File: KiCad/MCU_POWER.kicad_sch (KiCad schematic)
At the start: 12 parts, among them IC3 LDO40LPU33RY, J1 USB_B, J2 Jack-DC

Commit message: Board layout preleminary complete.
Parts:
- D3: footprint (none) -> Diode_SMD:D_SOD-123
- J2: footprint (none) -> Connector_BarrelJack:BarrelJack_CUI_PJ-063AH_Horizontal_CircularHoles
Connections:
- net RAW_FILTER: now reaches C11.1, D1.1 (K), D2.1 (K), D3.1 (K), FB1.1
- net USB_OUT: now reaches D1.2 (A), J1.1 (VBUS)
- net JACK_OUT: now reaches D2.2 (A), J2.1
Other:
- moved on the sheet: J2
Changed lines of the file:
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@@
   (no_connect (at 76.708 81.026))
   (no_connect (at 76.708 83.566))
-  (wire (pts (xy 77.724 111.252) (xy 76.2 111.252))
-    (stroke (width 0) (type default))
-  )
-  (wire (pts (xy 78.359 106.172) (xy 76.2 106.172))
+  (wire (pts (xy 74.803 106.172) (xy 78.359 106.172))
+    (stroke (width 0) (type default))
+  )
+  (wire (pts (xy 76.327 111.252) (xy 74.803 111.252))
     (stroke (width 0) (type default))
   )
@@
     (effects (font (size 3 3)) (justify left bottom))
   )
+  (label "JACK_OUT" (at 75.311 106.172 0) (fields_autoplaced)
+    (effects (font (size 0.7 0.7)) (justify left bottom))
+  )
+  (label "RAW_FILTER" (at 118.999 75.946 0) (fields_autoplaced)
+    (effects (font (size 1.27 1.27)) (justify left bottom))
+  )
   (label "EN" (at 160.528 73.406 0) (fields_autoplaced)
     (effects (font (size 0.8 0.8)) (justify left bottom))
+  )
+  (label "USB_OUT" (at 77.47 75.946 0) (fields_autoplaced)
+    (effects (font (size 0.7 0.7)) (justify left bottom))
   )
   (label "VIN" (at 160.02 75.946 0) (fields_autoplaced)
@@
       (effects (font (size 1.27 1.27)) (justify left))
     )
-    (property "Footprint" "" (at 100.076 79.756 0)
+    (property "Footprint" "Diode_SMD:D_SOD-123" (at 100.076 79.756 0)
       (effects (font (size 1.27 1.27)) hide)
     )
@@
   )
   (symbol (lib_id "Device:D_Schottky") (at 82.169 106.172 180) (unit 1)
-    (in_bom yes) (on_board yes) (dnp no) (fields_autoplaced)
-    (property "Reference" "D2" (at 82.4865 100.711 0)
-      (effects (font (size 1.27 1.27)))
-    )
-    (property "Value" "D_Schottky" (at 82.4865 103.251 0)
+    (in_bom yes) (on_board yes) (dnp no)
+    (property "Reference" "D2" (at 85.09 100.965 0)
+      (effects (font (size 1.27 1.27)))
+    )
+    (property "Value" "D_Schottky" (at 84.963 103.505 0)
       (effects (font (size 1.27 1.27)))
     )
@@
     )
   )
-  (symbol (lib_id "power:GND") (at 77.724 111.252 0) (unit 1)
-    (in_bom yes) (on_board yes) (dnp no) (fields_autoplaced)
-    (property "Reference" "#PWR014" (at 77.724 117.602 0)
-      (effects (font (size 1.27 1.27)) hide)
-    )
-    (property "Value" "GND" (at 77.724 115.824 0)
-      (effects (font (size 1.27 1.27)))
-    )
-    (property "Footprint" "" (at 77.724 111.252 0)
-      (effects (font (size 1.27 1.27)) hide)
-    )
-    (property "Datasheet" "" (at 77.724 111.252 0)
+  (symbol (lib_id "power:GND") (at 76.327 111.252 0) (unit 1)
+    (in_bom yes) (on_board yes) (dnp no) (fields_autoplaced)
+    (property "Reference" "#PWR014" (at 76.327 117.602 0)
+      (effects (font (size 1.27 1.27)) hide)
+    )
+    (property "Value" "GND" (at 76.327 115.824 0)
+      (effects (font (size 1.27 1.27)))
+    )
+    (property "Footprint" "" (at 76.327 111.252 0)
+      (effects (font (size 1.27 1.27)) hide)
+    )
+    (property "Datasheet" "" (at 76.327 111.252 0)
       (effects (font (size 1.27 1.27)) hide)
     )
@@
     )
   )
-  (symbol (lib_id "Connector:Jack-DC") (at 68.58 108.712 0) (unit 1)
-    (in_bom yes) (on_board yes) (dnp no) (fields_autoplaced)
-    (property "Reference" "J2" (at 68.58 101.219 0)
-      (effects (font (size 1.27 1.27)))
-    )
-    (property "Value" "Jack-DC" (at 68.58 103.759 0)
-      (effects (font (size 1.27 1.27)))
-    )
-    (property "Footprint" "" (at 69.85 109.728 0)
-      (effects (font (size 1.27 1.27)) hide)
-    )
-    (property "Datasheet" "~" (at 69.85 109.728 0)
-      (effects (font (size 1.27 1.27)) hide)
-    )
+  (symbol (lib_id "Connector:Jack-DC") (at 67.183 108.712 0) (unit 1)
+    (in_bom yes) (on_board yes) (dnp no) (fields_autoplaced)
+    (property "Reference" "J2" (at 67.183 101.219 0)
+      (effects (font (size 1.27 1.27)))
+    )
+    (property "Value" "Jack-DC" (at 67.183 103.759 0)
+      (effects (font (size 1.27 1.27)))
+    )
+    (property "Footprint" "Connector_BarrelJack:BarrelJack_CUI_PJ-063AH_Horizontal_CircularHoles" (at 68.453 109.728 0)
+      (effects (font (size 1.27 1.27)) hide)
+    )
+    (property "Datasheet" "~" (at 68.453 109.728 0)
+      (effects (font (size 1.27 1.27)) hide)
+    )

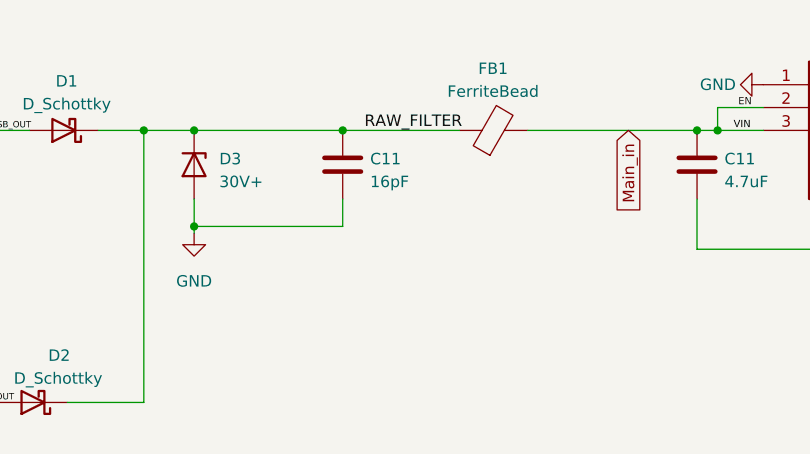
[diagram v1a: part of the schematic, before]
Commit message: Added some notes and extra ground vias.
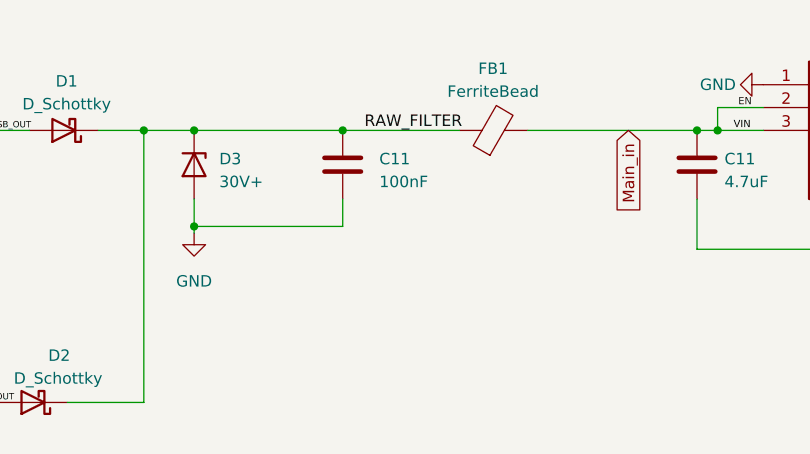
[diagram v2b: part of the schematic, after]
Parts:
- C11: value 16pF -> 100nF
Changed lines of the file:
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@@
   (symbol (lib_id "Device:C") (at 116.586 79.756 0) (unit 1)
     (in_bom yes) (on_board yes) (dnp no) (fields_autoplaced)
-    (property "Reference" "C11" (at 119.634 79.121 0)
+    (property "Reference" "C11" (at 120.65 79.121 0)
       (effects (font (size 1.27 1.27)) (justify left))
     )
-    (property "Value" "16pF" (at 119.634 81.661 0)
+    (property "Value" "100nF" (at 120.65 81.661 0)
       (effects (font (size 1.27 1.27)) (justify left))
     )

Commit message: Starting revision 1.1
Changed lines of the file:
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@@
   (junction (at 67.818 91.186) (diameter 0) (color 0 0 0 0)
+  )
+  (junction (at 194.564 75.946) (diameter 0) (color 0 0 0 0)
   )
   (junction (at 201.676 75.946) (diameter 0) (color 0 0 0 0)
@@
   (no_connect (at 76.708 81.026))
   (no_connect (at 76.708 83.566))
+  (wire (pts (xy 194.564 76.2) (xy 194.564 75.946))
+    (stroke (width 0) (type default))
+  )
   (wire (pts (xy 74.803 106.172) (xy 78.359 106.172))
     (stroke (width 0) (type default))
@@
     (stroke (width 0) (type default))
   )
-  (wire (pts (xy 201.676 75.946) (xy 197.358 75.946))
-    (stroke (width 0) (type default))
-  )
   (wire (pts (xy 67.818 91.186) (xy 69.088 91.186))
     (stroke (width 0) (type default))
@@
   )
   (wire (pts (xy 158.242 73.406) (xy 158.242 75.946))
+    (stroke (width 0) (type default))
+  )
+  (wire (pts (xy 197.358 75.946) (xy 201.676 75.946))
     (stroke (width 0) (type default))
   )
@@
   )
   (wire (pts (xy 178.562 89.154) (xy 178.562 88.646))
+    (stroke (width 0) (type default))
+  )
+  (wire (pts (xy 194.564 75.946) (xy 193.802 75.946))
     (stroke (width 0) (type default))
   )
@@
     (stroke (width 0) (type default))
   )
-  (wire (pts (xy 197.358 75.946) (xy 193.802 75.946))
+  (wire (pts (xy 197.358 75.946) (xy 194.564 75.946))
     (stroke (width 0) (type default))
   )
@@
     (effects (font (size 1.27 1.27)) (justify left bottom))
   )
-  (label "Vout" (at 199.39 75.946 0) (fields_autoplaced)
+  (label "Vout" (at 194.564 76.2 0) (fields_autoplaced)
     (effects (font (size 1.27 1.27)) (justify left bottom))
   )

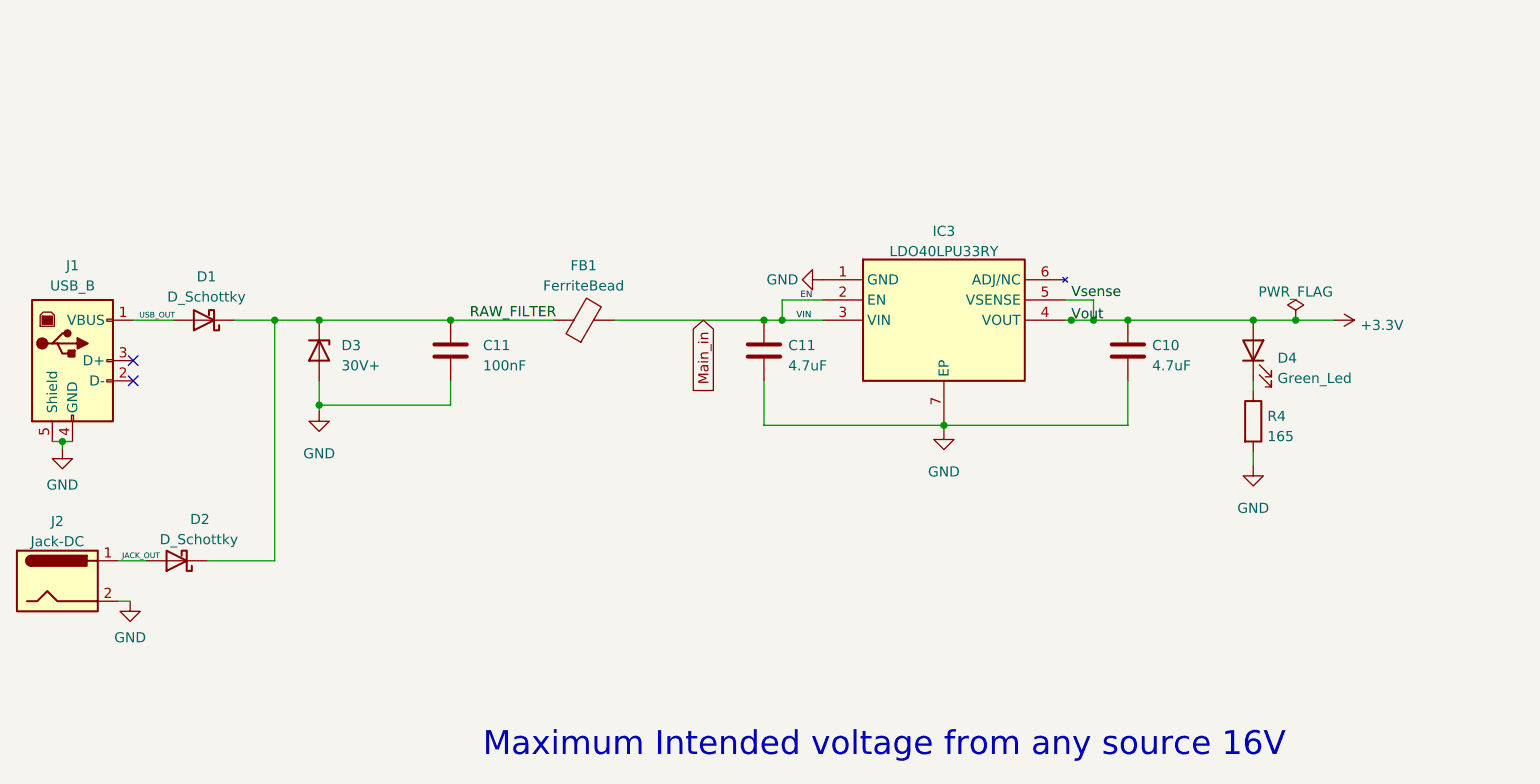
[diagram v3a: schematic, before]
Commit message: pushing ofr system reset
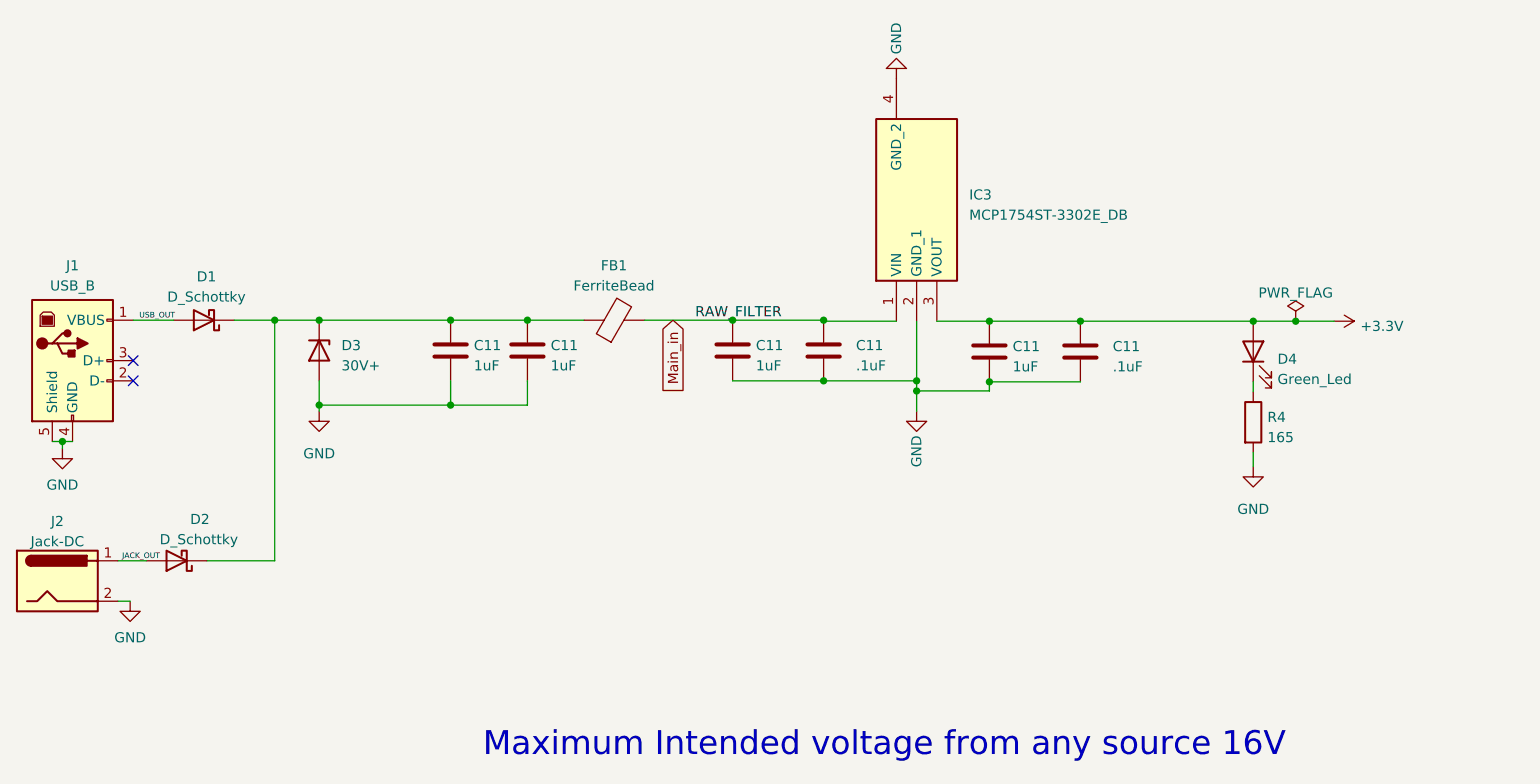
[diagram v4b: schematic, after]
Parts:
- removed C10, C11: 4.7uF, Capacitor_SMD:C_0603_1608Metric_Pad1.08x0.95mm_HandSolder, symbol Device:C
- removed C11: 100nF, Capacitor_SMD:C_0603_1608Metric_Pad1.08x0.95mm_HandSolder, symbol Device:C
- removed IC3: LDO40LPU33RY, Custom_eric:SON95P300X300X90-7N-D, symbol Custom_Eric:LDO40LPU33RY
- added C11 (x2): .1uF, Capacitor_SMD:C_0603_1608Metric_Pad1.08x0.95mm_HandSolder, symbol Device:C
- added C11 (x4): 1uF, Capacitor_SMD:C_0603_1608Metric_Pad1.08x0.95mm_HandSolder, symbol Device:C
- added IC3: MCP1754ST-3302E_DB, Custom_eric:MCP1754ST-3302E_DB, symbol Custom_eric:MCP1754ST-3302E_DB
- R4: footprint Resistor_SMD:R_0402_1005Metric_Pad0.72x0.64mm_HandSolder -> Resistor_SMD:R_0805_2012Metric_Pad1.20x1.40mm_HandSolder
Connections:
- net +3.3V: now also C11.1, C11.1, IC3.3 (VOUT)
- net GND: now also C11.2, C11.2, C11.2, C11.2, C11.2, C11.2, IC3.2 (GND_1), IC3.4 (GND_2)
- net Main_in: now also C11.1, C11.1, IC3.1 (VIN)
- net RAW_FILTER: no longer names the net of D1.1 (K), D2.1 (K), D3.1 (K), FB1.1
- net RAW_FILTER: now also C11.1, C11.1
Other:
- moved on the sheet: FB1

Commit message: Replaced pot.
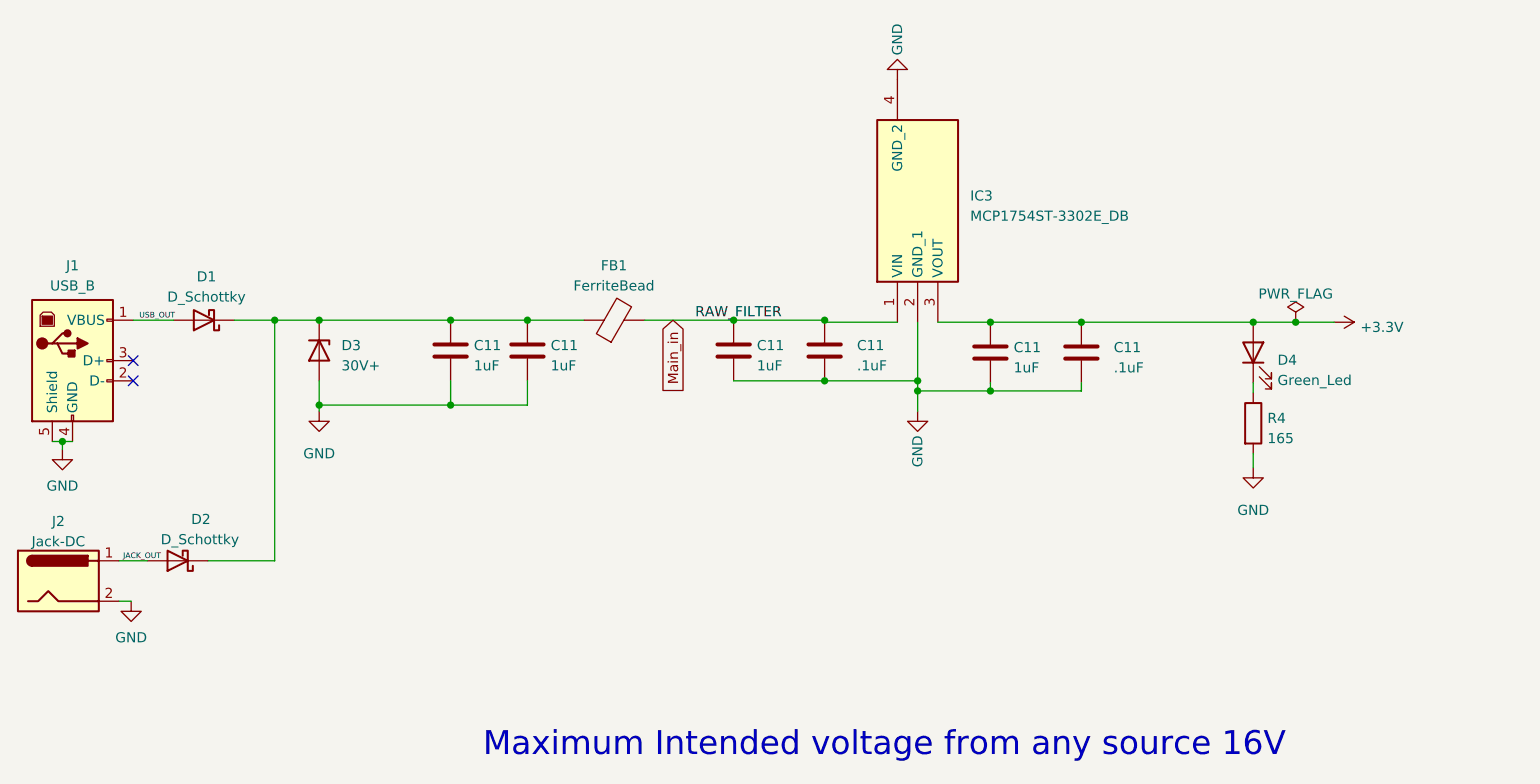
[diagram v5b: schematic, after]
